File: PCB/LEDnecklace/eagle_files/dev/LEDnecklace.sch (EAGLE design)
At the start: 6 parts, among them SW1 PCM12SMTR

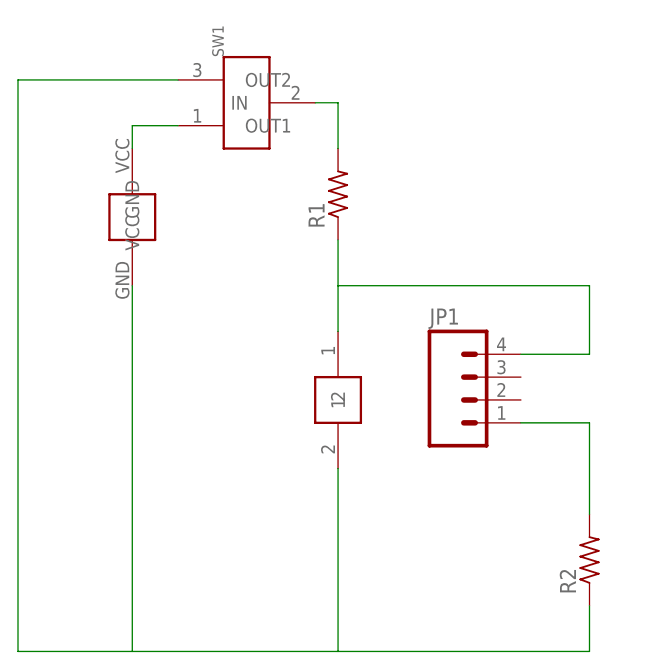
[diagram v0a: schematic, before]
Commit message: Develop version of LEDnecklace with XLampXBD and smaller coin cell (type 2016).
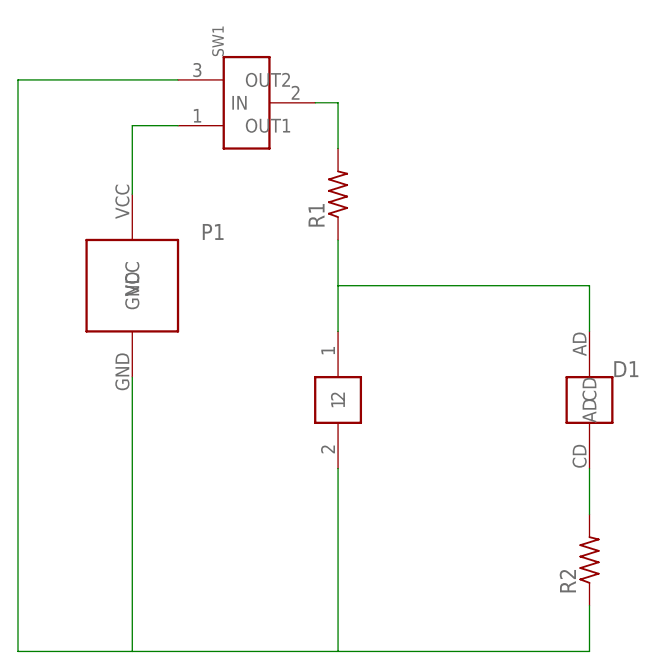
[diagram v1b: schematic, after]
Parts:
- removed JP1: (no value), SparkFun-Connectors:M04PTH
- added D1: XLAMP_XBD, freddyLibr:XLAMP_XBD
- P1: value (none) -> BC501SM_BATT_HOLD; device freddyLibr:BU2032SM-BT-GCT -> freddyLibr:BC501SM_BATT_HOLD
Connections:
- removed net N$16: JP1.4, PC1.1, R1.1
- new net N$4: D1.AD, PC1.1, R1.1
- net N$5: now also D1.CD; no longer JP1.1
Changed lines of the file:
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@@
 <part name="R1" library="resistor" deviceset="R-US_" device="R0603"/>
 <part name="R2" library="resistor" deviceset="R-US_" device="R0603"/>
-<part name="P1" library="freddyLibr" deviceset="BU2032SM-BT-GCT" device=""/>
 <part name="PC1" library="freddyLibr" deviceset="PDV-P8101" device=""/>
 <part name="SW1" library="freddyLibr" deviceset="PCM12SMTR" device=""/>
-<part name="JP1" library="SparkFun-Connectors" deviceset="M04" device="PTH"/>
+<part name="P1" library="freddyLibr" deviceset="BC501SM_BATT_HOLD" device=""/>
+<part name="D1" library="freddyLibr" deviceset="XLAMP_XBD" device=""/>
 </parts>
 <sheets>
@@
 <instance part="R1" gate="G$1" x="15.24" y="76.2" rot="R90"/>
 <instance part="R2" gate="G$1" x="43.18" y="35.56" rot="R90"/>
-<instance part="P1" gate="G$1" x="-7.62" y="73.66"/>
 <instance part="PC1" gate="G$1" x="15.24" y="53.34"/>
 <instance part="SW1" gate="G$1" x="5.08" y="86.36" rot="R90"/>
-<instance part="JP1" gate="G$1" x="30.48" y="53.34"/>
+<instance part="P1" gate="G$1" x="-7.62" y="66.04"/>
+<instance part="D1" gate="G$1" x="43.18" y="53.34"/>
 </instances>
 <busses>
@@
 <net name="N$2" class="0">
 <segment>
-<wire x1="-7.62" y1="66.04" x2="-7.62" y2="25.4" width="0.1524" layer="91"/>
+<wire x1="-20.32" y1="25.4" x2="-7.62" y2="25.4" width="0.1524" layer="91"/>
 <wire x1="-7.62" y1="25.4" x2="15.24" y2="25.4" width="0.1524" layer="91"/>
 <wire x1="15.24" y1="45.72" x2="15.24" y2="25.4" width="0.1524" layer="91"/>
@@
 <pinref part="R2" gate="G$1" pin="1"/>
 <wire x1="43.18" y1="30.48" x2="43.18" y2="25.4" width="0.1524" layer="91"/>
-<pinref part="P1" gate="G$1" pin="GND"/>
 <pinref part="PC1" gate="G$1" pin="2"/>
 <pinref part="SW1" gate="G$1" pin="OUT2"/>
 <wire x1="-2.54" y1="88.9" x2="-20.32" y2="88.9" width="0.1524" layer="91"/>
 <wire x1="-20.32" y1="88.9" x2="-20.32" y2="25.4" width="0.1524" layer="91"/>
-<wire x1="-20.32" y1="25.4" x2="-7.62" y2="25.4" width="0.1524" layer="91"/>
+<pinref part="P1" gate="G$1" pin="GND"/>
+<wire x1="-7.62" y1="55.88" x2="-7.62" y2="25.4" width="0.1524" layer="91"/>
 </segment>
 </net>
@@
 </segment>
 </net>
-<net name="N$6" class="0">
+<net name="N$3" class="0">
 <segment>
+<pinref part="SW1" gate="G$1" pin="OUT1"/>
 <pinref part="P1" gate="G$1" pin="VCC"/>
-<wire x1="-7.62" y1="81.28" x2="-7.62" y2="83.82" width="0.1524" layer="91"/>
-<pinref part="SW1" gate="G$1" pin="OUT1"/>
-<wire x1="-7.62" y1="83.82" x2="-2.54" y2="83.82" width="0.1524" layer="91"/>
+<wire x1="-2.54" y1="83.82" x2="-7.62" y2="83.82" width="0.1524" layer="91"/>
+<wire x1="-7.62" y1="83.82" x2="-7.62" y2="76.2" width="0.1524" layer="91"/>
 </segment>
 </net>
-<net name="N$16" class="0">
+<net name="N$4" class="0">
 <segment>
+<pinref part="PC1" gate="G$1" pin="1"/>
 <pinref part="R1" gate="G$1" pin="1"/>
 <wire x1="15.24" y1="71.12" x2="15.24" y2="66.04" width="0.1524" layer="91"/>
-<pinref part="PC1" gate="G$1" pin="1"/>
-<pinref part="JP1" gate="G$1" pin="4"/>
+<pinref part="D1" gate="G$1" pin="AD"/>
 <wire x1="15.24" y1="66.04" x2="15.24" y2="60.96" width="0.1524" layer="91"/>
-<wire x1="35.56" y1="58.42" x2="43.18" y2="58.42" width="0.1524" layer="91"/>
-<wire x1="43.18" y1="58.42" x2="43.18" y2="66.04" width="0.1524" layer="91"/>
-<wire x1="43.18" y1="66.04" x2="15.24" y2="66.04" width="0.1524" layer="91"/>
+<wire x1="15.24" y1="66.04" x2="43.18" y2="66.04" width="0.1524" layer="91"/>
+<wire x1="43.18" y1="66.04" x2="43.18" y2="60.96" width="0.1524" layer="91"/>
 </segment>
 </net>
@@
 <segment>
 <pinref part="R2" gate="G$1" pin="2"/>
-<wire x1="43.18" y1="40.64" x2="43.18" y2="50.8" width="0.1524" layer="91"/>
-<pinref part="JP1" gate="G$1" pin="1"/>
-<wire x1="43.18" y1="50.8" x2="35.56" y2="50.8" width="0.1524" layer="91"/>
+<pinref part="D1" gate="G$1" pin="CD"/>
+<wire x1="43.18" y1="40.64" x2="43.18" y2="45.72" width="0.1524" layer="91"/>
 </segment>
 </net>

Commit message: Change border around LED. Hopefully more visible.
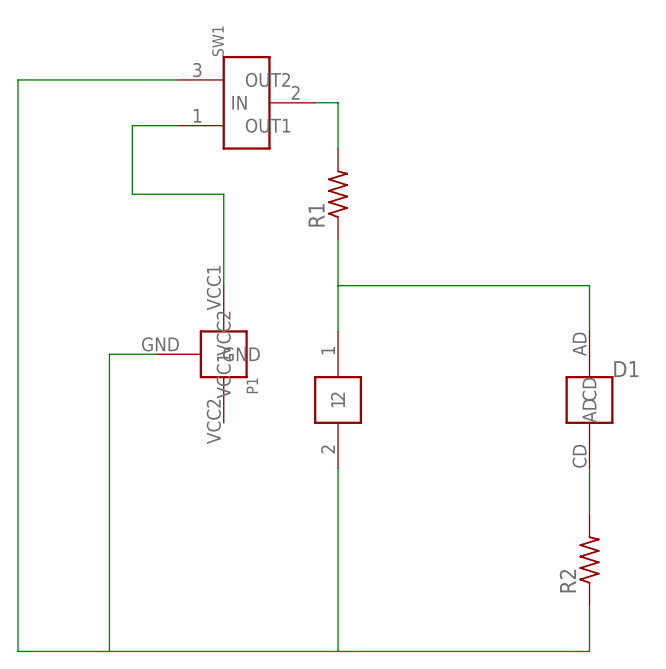
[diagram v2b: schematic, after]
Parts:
- P1: value BC501SM_BATT_HOLD -> CR1220; device freddyLibr:BC501SM_BATT_HOLD -> freddyLibr:CR1220
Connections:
- net N$3: now also P1.VCC1; no longer P1.VCC
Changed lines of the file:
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@@
 <part name="PC1" library="freddyLibr" deviceset="PDV-P8101" device=""/>
 <part name="SW1" library="freddyLibr" deviceset="PCM12SMTR" device=""/>
-<part name="P1" library="freddyLibr" deviceset="BC501SM_BATT_HOLD" device=""/>
+<part name="P1" library="freddyLibr" deviceset="CR1220" device=""/>
 <part name="D1" library="freddyLibr" deviceset="XLAMP_XBD" device=""/>
 </parts>
@@
 <instance part="PC1" gate="G$1" x="15.24" y="53.34"/>
 <instance part="SW1" gate="G$1" x="5.08" y="86.36" rot="R90"/>
-<instance part="P1" gate="G$1" x="-7.62" y="66.04"/>
+<instance part="P1" gate="G$1" x="2.54" y="58.42" rot="R270"/>
 <instance part="D1" gate="G$1" x="43.18" y="53.34"/>
 </instances>
@@
 <net name="N$2" class="0">
 <segment>
-<wire x1="-20.32" y1="25.4" x2="-7.62" y2="25.4" width="0.1524" layer="91"/>
-<wire x1="-7.62" y1="25.4" x2="15.24" y2="25.4" width="0.1524" layer="91"/>
+<wire x1="-20.32" y1="25.4" x2="-10.16" y2="25.4" width="0.1524" layer="91"/>
+<wire x1="-10.16" y1="25.4" x2="15.24" y2="25.4" width="0.1524" layer="91"/>
 <wire x1="15.24" y1="45.72" x2="15.24" y2="25.4" width="0.1524" layer="91"/>
 <wire x1="15.24" y1="25.4" x2="43.18" y2="25.4" width="0.1524" layer="91"/>
@@
 <wire x1="-2.54" y1="88.9" x2="-20.32" y2="88.9" width="0.1524" layer="91"/>
 <wire x1="-20.32" y1="88.9" x2="-20.32" y2="25.4" width="0.1524" layer="91"/>
+<wire x1="-5.08" y1="58.42" x2="-10.16" y2="58.42" width="0.1524" layer="91"/>
+<wire x1="-10.16" y1="58.42" x2="-10.16" y2="25.4" width="0.1524" layer="91"/>
 <pinref part="P1" gate="G$1" pin="GND"/>
-<wire x1="-7.62" y1="55.88" x2="-7.62" y2="25.4" width="0.1524" layer="91"/>
 </segment>
 </net>
@@
 <segment>
 <pinref part="SW1" gate="G$1" pin="OUT1"/>
-<pinref part="P1" gate="G$1" pin="VCC"/>
 <wire x1="-2.54" y1="83.82" x2="-7.62" y2="83.82" width="0.1524" layer="91"/>
-<wire x1="-7.62" y1="83.82" x2="-7.62" y2="76.2" width="0.1524" layer="91"/>
+<wire x1="2.54" y1="66.04" x2="2.54" y2="76.2" width="0.1524" layer="91"/>
+<wire x1="2.54" y1="76.2" x2="-7.62" y2="76.2" width="0.1524" layer="91"/>
+<wire x1="-7.62" y1="76.2" x2="-7.62" y2="83.82" width="0.1524" layer="91"/>
+<pinref part="P1" gate="G$1" pin="VCC1"/>
 </segment>
 </net>
@@
 <pinref part="R1" gate="G$1" pin="1"/>
 <wire x1="15.24" y1="71.12" x2="15.24" y2="66.04" width="0.1524" layer="91"/>
-<pinref part="D1" gate="G$1" pin="AD"/>
 <wire x1="15.24" y1="66.04" x2="15.24" y2="60.96" width="0.1524" layer="91"/>
 <wire x1="15.24" y1="66.04" x2="43.18" y2="66.04" width="0.1524" layer="91"/>
 <wire x1="43.18" y1="66.04" x2="43.18" y2="60.96" width="0.1524" layer="91"/>
+<pinref part="D1" gate="G$1" pin="AD"/>
 </segment>
 </net>
@@
 <segment>
 <pinref part="R2" gate="G$1" pin="2"/>
+<wire x1="43.18" y1="40.64" x2="43.18" y2="45.72" width="0.1524" layer="91"/>
 <pinref part="D1" gate="G$1" pin="CD"/>
-<wire x1="43.18" y1="40.64" x2="43.18" y2="45.72" width="0.1524" layer="91"/>
 </segment>
 </net>
